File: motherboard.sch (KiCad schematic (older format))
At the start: 90 parts, among them P1 CONN_02X08, U1 STM32F411-LQFP64, U10 74LS125, U11 74LS125, U12 74LS125, U13 74LS125, U14 PCA9517A, U15 PCA9517A, U16 74LS125, U17 74LS125, U2 STM32F411-LQFP64, U3 AP7313, U4 74LS00, U5 74LS125, U6 FM25V20A-G, U7 FM25V20A-G, U8 FM25V20A-G, U9 FM25V20A-G, Y1 32k, Y2 8M(16pF), Y3 32k, Y4 8M(16pF)

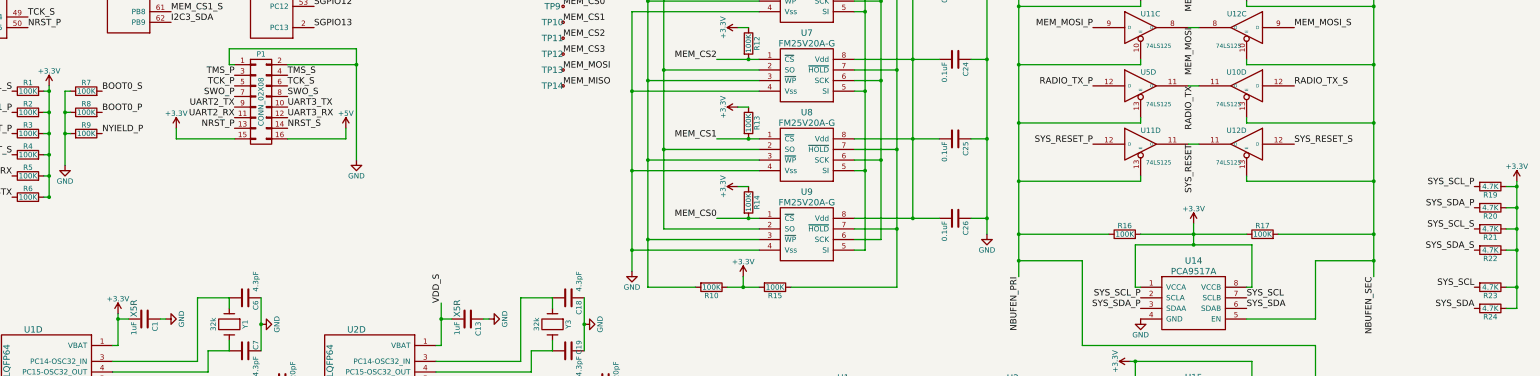
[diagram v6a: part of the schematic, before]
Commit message: Placed all components
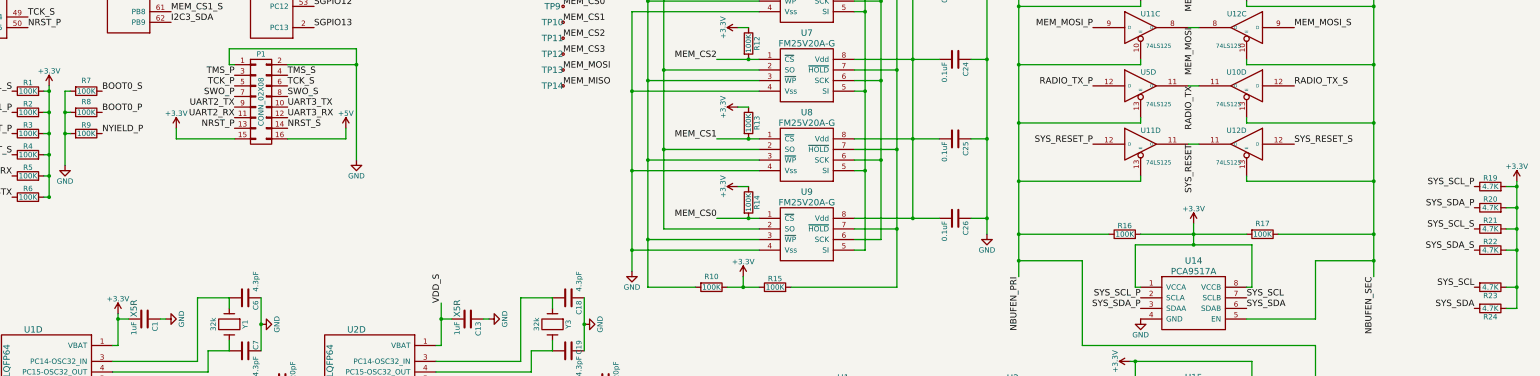
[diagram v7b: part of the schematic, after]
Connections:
- net +3V3: now also R15.1, R17.2, R19.2, R20.2, R21.2, R22.2; no longer R15.2, R17.1, R19.1, R20.1, R21.1, R22.1
- net BOOT0_P: now also R8.1; no longer R8.2
- net BOOT0_S: now also R7.1; no longer R7.2
- net GND: now also R7.2, R8.2; no longer R7.1, R8.1
- net NBUFEN_SEC: now also R17.1; no longer R17.2
- net SYS_SCL_P: now also R19.1; no longer R19.2
- net SYS_SCL_S: now also R21.1; no longer R21.2
- net SYS_SDA_P: now also R20.1; no longer R20.2
- net SYS_SDA_S: now also R22.1; no longer R22.2
- net at U6.7 (~HOLD), U7.7 (~HOLD), U8.7 (~HOLD)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: now also R15.2; no longer R15.1
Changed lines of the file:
@@
 U 1 1 56B9204C
 P 13100 6750
-F 0 "R17" V 13180 6750 50  0000 C CNN
+F 0 "R17" V 13000 6750 50  0000 C CNN
 F 1 "100K" V 13100 6750 50  0000 C CNN
 F 2 "Resistors_SMD:R_0805_HandSoldering" V 13030 6750 30  0001 C CNN
 F 3 "" H 13100 6750 30  0000 C CNN
 	1    13100 6750
-	0    -1   -1   0
+	0    1    1    0
 $EndComp
 $Comp
@@
 U 1 1 56E68F3A
 P 2000 5600
-F 0 "R8" V 2080 5600 50  0000 C CNN
+F 0 "R8" V 1900 5600 50  0000 C CNN
 F 1 "100K" V 2000 5600 50  0000 C CNN
 F 2 "Resistors_SMD:R_0805_HandSoldering" V 1930 5600 30  0001 C CNN
 F 3 "" H 2000 5600 30  0000 C CNN
 	1    2000 5600
-	0    -1   -1   0
+	0    1    1    0
 $EndComp
 $Comp
@@
 U 1 1 56E690F6
 P 2000 5400
-F 0 "R7" V 2080 5400 50  0000 C CNN
+F 0 "R7" V 1900 5400 50  0000 C CNN
 F 1 "100K" V 2000 5400 50  0000 C CNN
 F 2 "Resistors_SMD:R_0805_HandSoldering" V 1930 5400 30  0001 C CNN
 F 3 "" H 2000 5400 30  0000 C CNN
 	1    2000 5400
-	0    -1   -1   0
+	0    1    1    0
 $EndComp
 Text Label 2150 5600 0    60   ~ 0
@@
 F 3 "" H 15250 6300 30  0000 C CNN
 	1    15250 6300
-	0    1    1    0
+	0    -1   -1   0
 $EndComp
 $Comp
@@
 F 3 "" H 15250 6500 30  0000 C CNN
 	1    15250 6500
-	0    1    1    0
+	0    -1   -1   0
 $EndComp
 $Comp
@@
 F 3 "" H 15250 6700 30  0000 C CNN
 	1    15250 6700
-	0    1    1    0
+	0    -1   -1   0
 $EndComp
 $Comp
@@
 F 3 "" H 15250 6900 30  0000 C CNN
 	1    15250 6900
-	0    1    1    0
+	0    -1   -1   0
 $EndComp
 $Comp
@@
 U 1 1 56FFBA91
 P 7900 7250
-F 0 "R10" V 7980 7250 50  0000 C CNN
+F 0 "R10" V 7800 7250 50  0000 C CNN
 F 1 "100K" V 7900 7250 50  0000 C CNN
 F 2 "Resistors_SMD:R_0805_HandSoldering" V 7830 7250 30  0001 C CNN
@@
 F 3 "" H 8500 7250 30  0000 C CNN
 	1    8500 7250
-	0    1    1    0
-$EndComp
-$Comp
+	0    -1   -1   0
+$EndComp
+$Comp

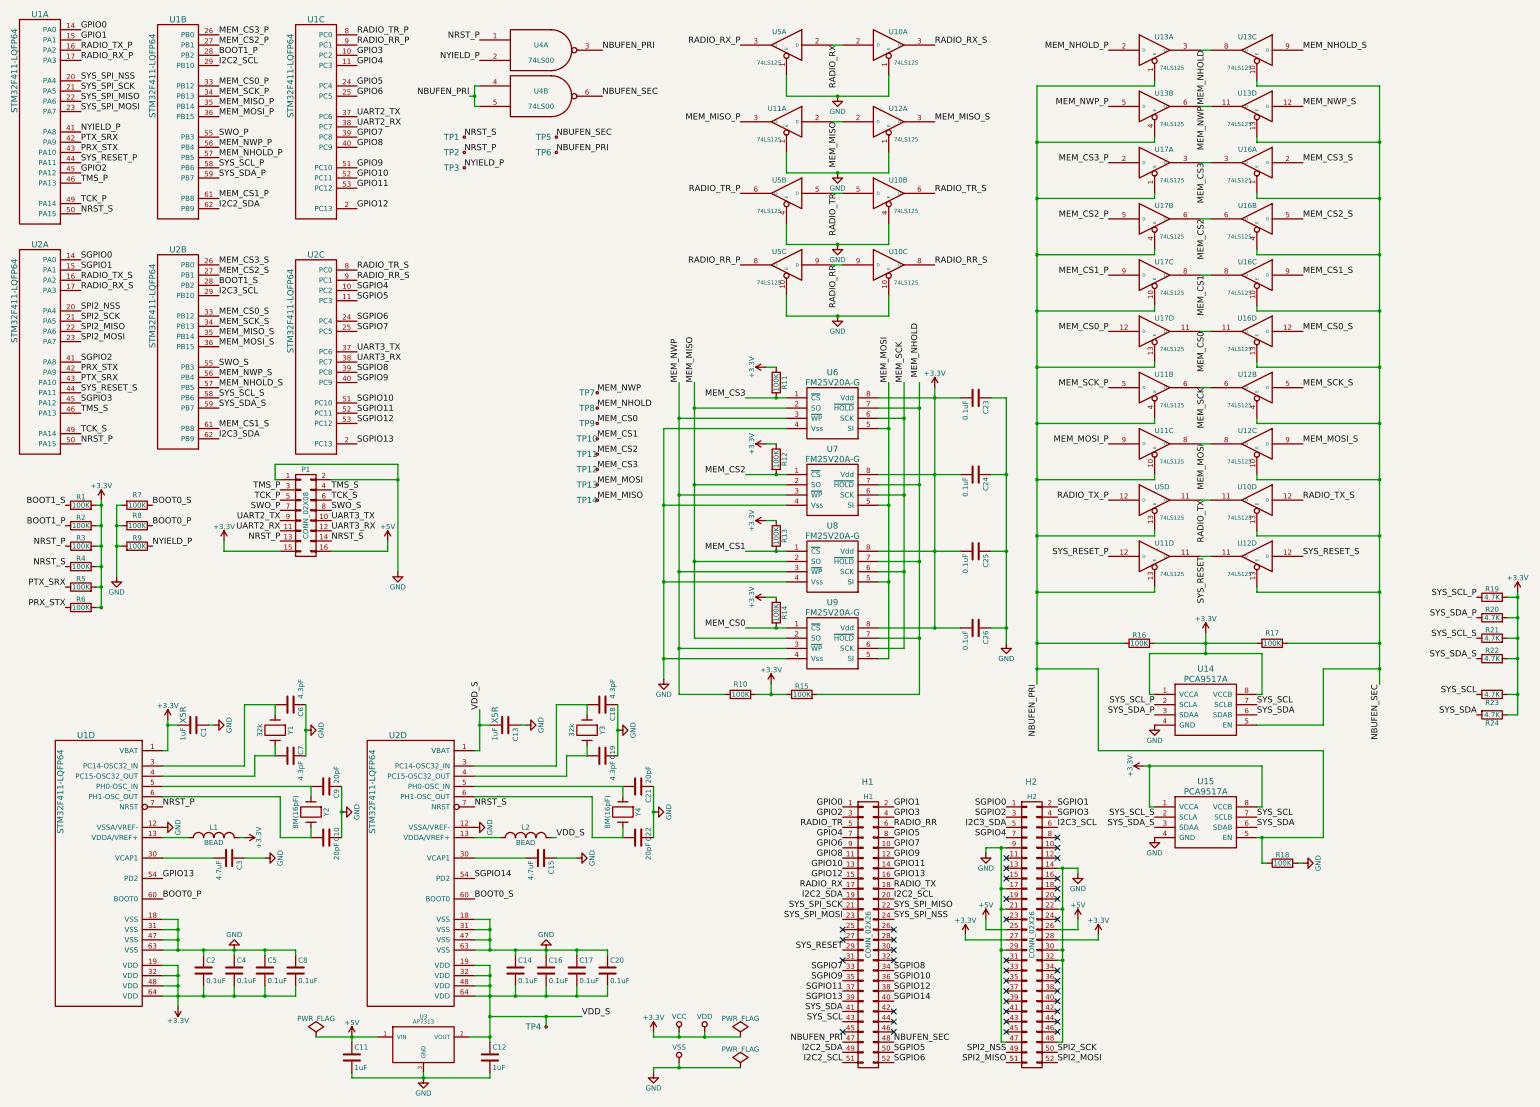
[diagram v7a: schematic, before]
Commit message: Routed P1 High-speed signals
- Main UART
- Main I2C
- Mem SPI
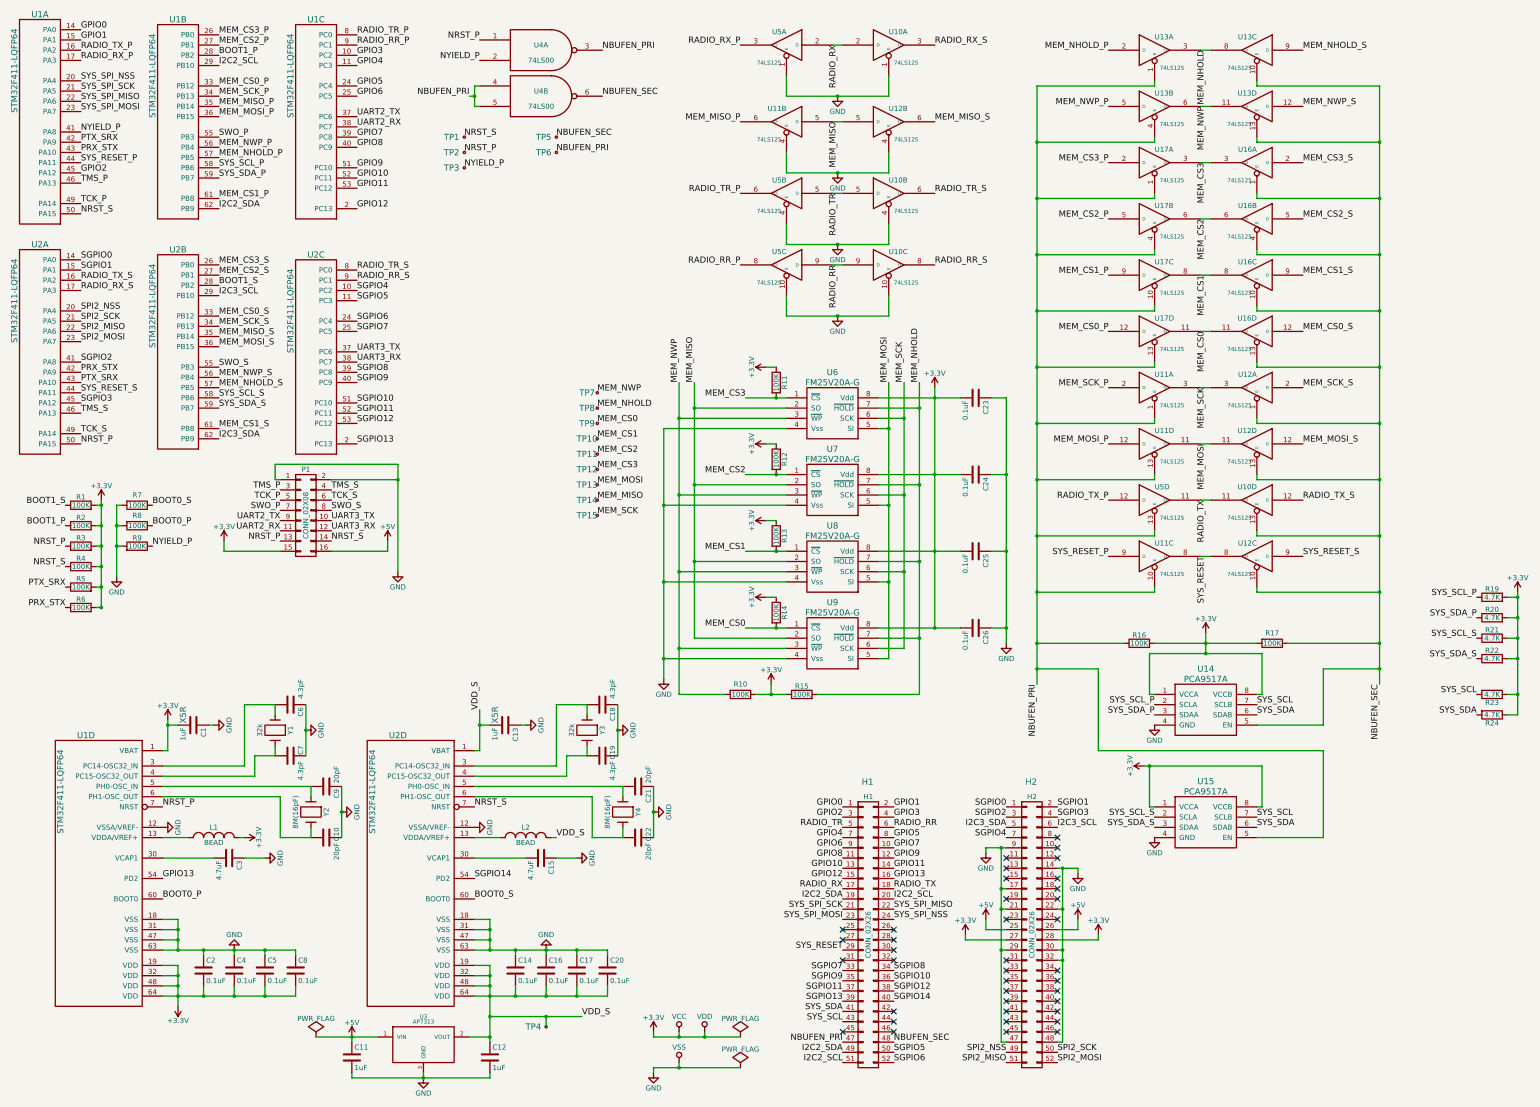
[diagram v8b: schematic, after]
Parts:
- removed R18: 100K, Resistors_SMD:R_0805_HandSoldering, symbol R
- added TP15: TP, motherboard:TP_0603, symbol TP
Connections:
- net GND: now also U11.4 (E), U12.4 (E); no longer U11.1 (E), U12.1 (E)
- net MEM_MISO: now also U11.5 (D), U12.5 (D); no longer U11.2 (D), U12.2 (D)
- net MEM_MISO_P: now also U11.6 (O); no longer U11.3 (O)
- net MEM_MISO_S: now also U12.6 (O); no longer U12.3 (O)
- net MEM_MOSI: now also U11.11 (O), U12.11 (O); no longer U11.8 (O), U12.8 (O)
- net MEM_MOSI_P: now also U11.12 (D); no longer U11.9 (D)
- net MEM_MOSI_S: now also U12.12 (D); no longer U12.9 (D)
- net MEM_NHOLD: now also R15.2, U6.7 (~HOLD), U7.7 (~HOLD), U8.7 (~HOLD), U9.7 (~HOLD)
- net MEM_SCK: now also U11.3 (O), U12.3 (O), TP15.1; no longer U11.6 (O), U12.6 (O)
- net MEM_SCK_P: now also U11.2 (D); no longer U11.5 (D)
- net MEM_SCK_S: now also U12.2 (D); no longer U12.5 (D)
- net NBUFEN_PRI: now also U11.1 (E), U11.10 (E), U11.13 (E); no longer U11.10 (E), U11.13 (E), U11.4 (E)
- net NBUFEN_SEC: now also U12.1 (E), U12.10 (E), U12.13 (E); no longer U12.10 (E), U12.13 (E), U12.4 (E)
- net SYS_RESET: now also U11.8 (O), U12.8 (O); no longer U11.11 (O), U12.11 (O)
- net SYS_RESET_P: now also U11.9 (D); no longer U11.12 (D)
- net SYS_RESET_S: now also U12.9 (D); no longer U12.12 (D)
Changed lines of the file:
@@
 	1    0    0    -1
 $EndComp
-Text Label 9650 4150 1    60   ~ 0
+Text Label 9650 4200 1    60   ~ 0
 MEM_NHOLD
 Text Label 9500 4200 1    60   ~ 0
@@
 	1    0    0    -1
 $EndComp
-$Comp
-L R R18
-U 1 1 56EF0DD7
-P 13200 8900
-F 0 "R18" V 13280 8900 50  0000 C CNN
-F 1 "100K" V 13200 8900 50  0000 C CNN
-F 2 "Resistors_SMD:R_0805_HandSoldering" V 13130 8900 30  0001 C CNN
-F 3 "" H 13200 8900 30  0000 C CNN
-	1    13200 8900
-	0    -1   -1   0
-$EndComp
-$Comp
-L GND #PWR034
-U 1 1 56EF0DDD
-P 13400 8900
-F 0 "#PWR034" H 13400 8650 50  0001 C CNN
-F 1 "GND" H 13400 8750 50  0000 C CNN
-F 2 "" H 13400 8900 60  0000 C CNN
-F 3 "" H 13400 8900 60  0000 C CNN
-	1    13400 8900
-	0    -1   -1   0
-$EndComp
 Text Label 11950 8450 2    60   ~ 0
 SYS_SCL_S
@@
 SYS_SDA_S
 $Comp
-L GND #PWR035
+L GND #PWR034
 U 1 1 56EF0DEA
 P 11950 8650
-F 0 "#PWR035" H 11950 8400 50  0001 C CNN
+F 0 "#PWR034" H 11950 8400 50  0001 C CNN
 F 1 "GND" H 11950 8500 50  0000 C CNN
 F 2 "" H 11950 8650 60  0000 C CNN
@@
 SYS_SDA
 $Comp
-L +3.3V #PWR036
+L +3.3V #PWR035
 U 1 1 56EF1331
 P 11850 7950
-F 0 "#PWR036" H 11850 7800 50  0001 C CNN
+F 0 "#PWR035" H 11850 7800 50  0001 C CNN
 F 1 "+3.3V" H 11850 8090 50  0000 C CNN
 F 2 "" H 11850 7950 60  0000 C CNN
@@
 $EndComp
 $Comp
-L +3.3V #PWR037
+L +3.3V #PWR036
 U 1 1 56F035F5
 P 15500 6250
-F 0 "#PWR037" H 15500 6100 50  0001 C CNN
+F 0 "#PWR036" H 15500 6100 50  0001 C CNN
 F 1 "+3.3V" H 15500 6390 50  0000 C CNN
 F 2 "" H 15500 6250 60  0000 C CNN
@@
 $Comp
 L 74LS125 U11
-U 1 1 56F0C25F
+U 2 1 56F0C25F
 P 8350 1650
 F 0 "U11" H 8350 1750 50  0000 L BNN
@@
 F 2 "Housings_SOIC:SOIC-14_3.9x8.7mm_Pitch1.27mm" H 8350 1650 60  0001 C CNN
 F 3 "" H 8350 1650 60  0000 C CNN
-	1    8350 1650
+	2    8350 1650
 	-1   0    0    -1
 $EndComp
 $Comp
 L 74LS125 U12
-U 1 1 56F0C346
+U 2 1 56F0C346
 P 9350 1650
 F 0 "U12" H 9350 1750 50  0000 L BNN
@@
 F 2 "Housings_SOIC:SOIC-14_3.9x8.7mm_Pitch1.27mm" H 9350 1650 60  0001 C CNN
 F 3 "" H 9350 1650 60  0000 C CNN
-	1    9350 1650
+	2    9350 1650
 	1    0    0    -1
 $EndComp
@@
 $Comp
 L 74LS125 U11
-U 2 1 56F1DA36
+U 1 1 56F1DA36
 P 11950 4250
 F 0 "U11" H 11950 4350 50  0000 L BNN
@@
 F 2 "Housings_SOIC:SOIC-14_3.9x8.7mm_Pitch1.27mm" H 11950 4250 60  0001 C CNN
 F 3 "" H 11950 4250 60  0000 C CNN
-	2    11950 4250
+	1    11950 4250
 	1    0    0    -1
 $EndComp
 $Comp
 L 74LS125 U11
-U 3 1 56F1DB80
+U 4 1 56F1DB80
 P 11950 4800
 F 0 "U11" H 11950 4900 50  0000 L BNN
@@
 F 2 "Housings_SOIC:SOIC-14_3.9x8.7mm_Pitch1.27mm" H 11950 4800 60  0001 C CNN
 F 3 "" H 11950 4800 60  0000 C CNN
-	3    11950 4800
+	4    11950 4800
 	1    0    0    -1
 $EndComp
@@
 $Comp
 L 74LS125 U12
-U 2 1 56F39A21
+U 1 1 56F39A21
 P 12950 4250
 F 0 "U12" H 12950 4350 50  0000 L BNN
@@
 F 2 "Housings_SOIC:SOIC-14_3.9x8.7mm_Pitch1.27mm" H 12950 4250 60  0001 C CNN
 F 3 "" H 12950 4250 60  0000 C CNN
-	2    12950 4250
+	1    12950 4250
 	-1   0    0    -1
 $EndComp
 $Comp
 L 74LS125 U12
-U 3 1 56F39B79
+U 4 1 56F39B79
 P 12950 4800
 F 0 "U12" H 12950 4900 50  0000 L BNN
@@
 F 2 "Housings_SOIC:SOIC-14_3.9x8.7mm_Pitch1.27mm" H 12950 4800 60  0001 C CNN
 F 3 "" H 12950 4800 60  0000 C CNN
-	3    12950 4800
+	4    12950 4800
 	-1   0    0    -1
 $EndComp
@@
 $Comp
 L 74LS125 U11
-U 4 1 56F44FCB
+U 3 1 56F44FCB
 P 11950 5900
 F 0 "U11" H 11950 6000 50  0000 L BNN
@@
 F 2 "Housings_SOIC:SOIC-14_3.9x8.7mm_Pitch1.27mm" H 11950 5900 60  0001 C CNN
 F 3 "" H 11950 5900 60  0000 C CNN
-	4    11950 5900
+	3    11950 5900
 	1    0    0    -1
 $EndComp
 $Comp
 L 74LS125 U12
-U 4 1 56F45134
+U 3 1 56F45134
 P 12950 5900
 F 0 "U12" H 12950 6000 50  0000 L BNN
@@
 F 2 "Housings_SOIC:SOIC-14_3.9x8.7mm_Pitch1.27mm" H 12950 5900 60  0001 C CNN
 F 3 "" H 12950 5900 60  0000 C CNN
-	4    12950 5900
+	3    12950 5900
 	-1   0    0    -1
 $EndComp
@@
 SYS_RESET
 $Comp
-L +3.3V #PWR038
+L +3.3V #PWR037
 U 1 1 56B92E1E
 P 12450 6650
-F 0 "#PWR038" H 12450 6500 50  0001 C CNN
+F 0 "#PWR037" H 12450 6500 50  0001 C CNN
 F 1 "+3.3V" H 12450 6790 50  0000 C CNN
 F 2 "" H 12450 6650 60  0000 C CNN
@@
 NRST_P
 $Comp
-L GND #PWR039
+L GND #PWR038
 U 1 1 56F7245E
 P 4550 6050
-F 0 "#PWR039" H 4550 5800 50  0001 C CNN
+F 0 "#PWR038" H 4550 5800 50  0001 C CNN
 F 1 "GND" H 4550 5900 50  0000 C CNN
 F 2 "" H 4550 6050 60  0000 C CNN
@@
 SGPIO14
 $Comp
-L +5V #PWR040
+L +5V #PWR039
 U 1 1 56FC214F
 P 4100 10600
-F 0 "#PWR040" H 4100 10450 50  0001 C CNN
+F 0 "#PWR039" H 4100 10450 50  0001 C CNN
 F 1 "+5V" H 4100 10740 50  0000 C CNN
 F 2 "" H 4100 10600 60  0000 C CNN
@@
 $EndComp
 $Comp
-L PWR_FLAG #FLG041
+L PWR_FLAG #FLG040
 U 1 1 56FDA5CD
 P 7900 10600
-F 0 "#FLG041" H 7900 10695 50  0001 C CNN
+F 0 "#FLG040" H 7900 10695 50  0001 C CNN
 F 1 "PWR_FLAG" H 7900 10780 50  0000 C CNN
 F 2 "" H 7900 10600 60  0000 C CNN
@@
 $EndComp
 $Comp
-L PWR_FLAG #FLG042
+L PWR_FLAG #FLG041
 U 1 1 56FDB2EA
 P 7900 10900
-F 0 "#FLG042" H 7900 10995 50  0001 C CNN
+F 0 "#FLG041" H 7900 10995 50  0001 C CNN
 F 1 "PWR_FLAG" H 7900 11080 50  0000 C CNN
 F 2 "" H 7900 10900 60  0000 C CNN
@@
 $EndComp
 $Comp
-L PWR_FLAG #FLG043
+L PWR_FLAG #FLG042
 U 1 1 56FE0079
 P 3750 10600
-F 0 "#FLG043" H 3750 10695 50  0001 C CNN
+F 0 "#FLG042" H 3750 10695 50  0001 C CNN
 F 1 "PWR_FLAG" H 3750 10780 50  0000 C CNN
 F 2 "" H 3750 10600 60  0000 C CNN
@@
 $EndComp
 $Comp
-L +3.3V #PWR044
+L +3.3V #PWR043
 U 1 1 56FFD810
 P 8200 7150
-F 0 "#PWR044" H 8200 7000 50  0001 C CNN
+F 0 "#PWR043" H 8200 7000 50  0001 C CNN
 F 1 "+3.3V" H 8200 7290 50  0000 C CNN
 F 2 "" H 8200 7150 60  0000 C CNN
@@
 RADIO_RR_S
 $Comp
-L GND #PWR045
+L GND #PWR044
 U 1 1 583EB3FD
 P 8850 2850
-F 0 "#PWR045" H 8850 2600 50  0001 C CNN
+F 0 "#PWR044" H 8850 2600 50  0001 C CNN
 F 1 "GND" H 8850 2700 50  0000 C CNN
 F 2 "" H 8850 2850 60  0000 C CNN
@@
 $EndComp
 $Comp
-L GND #PWR046
+L GND #PWR045
 U 1 1 583EB403
 P 8850 3550
-F 0 "#PWR046" H 8850 3300 50  0001 C CNN
+F 0 "#PWR045" H 8850 3300 50  0001 C CNN
 F 1 "GND" H 8850 3400 50  0000 C CNN
 F 2 "" H 8850 3550 60  0000 C CNN
@@
 $EndComp
 $Comp
-L +3.3V #PWR047
+L +3.3V #PWR046
 U 1 1 5843537A
 P 2850 5750
-F 0 "#PWR047" H 2850 5600 50  0001 C CNN
+F 0 "#PWR046" H 2850 5600 50  0001 C CNN
 F 1 "+3.3V" H 2850 5890 50  0000 C CNN
 F 2 "" H 2850 5750 50  0000 C CNN
@@
 $EndComp
 $Comp
-L +5V #PWR048
+L +5V #PWR047
 U 1 1 5843721B
 P 4450 5750
-F 0 "#PWR048" H 4450 5600 50  0001 C CNN
+F 0 "#PWR047" H 4450 5600 50  0001 C CNN
 F 1 "+5V" H 4450 5890 50  0000 C CNN
 F 2 "" H 4450 5750 50  0000 C CNN
@@
 	11400 7000 11400 7800
 Wire Wire Line
-	13000 8900 13000 8650
-Wire Wire Line
 	12950 8650 13600 8650
 Wire Wire Line
@@
 	13000 7950 11850 7950
 Connection ~ 11900 7950
-Wire Wire Line
-	13000 8900 13050 8900
-Connection ~ 13000 8650
 Wire Wire Line
 	13600 7000 14150 7000
@@
 	6000 10400 6000 10500
 Connection ~ 6000 10400
-Wire Wire Line
-	13350 8900 13400 8900
 Connection ~ 7550 10600
 Connection ~ 7300 10900
@@
 Connection ~ 10450 8750
 $Comp
-L GND #PWR049
+L GND #PWR048
 U 1 1 5844E13A
 P 10300 8800
-F 0 "#PWR049" H 10300 8550 50  0001 C CNN
+F 0 "#PWR048" H 10300 8550 50  0001 C CNN
 F 1 "GND" H 10300 8650 50  0000 C CNN
 F 2 "" H 10300 8800 60  0000 C CNN
@@
 	11000 8950 11200 8950
 $Comp
-L GND #PWR050
+L GND #PWR049
 U 1 1 5844E529
 P 11200 9000
-F 0 "#PWR050" H 11200 8750 50  0001 C CNN
+F 0 "#PWR049" H 11200 8750 50  0001 C CNN
 F 1 "GND" H 11200 8850 50  0000 C CNN
 F 2 "" H 11200 9000 60  0000 C CNN
@@
 NoConn ~ 11000 9450
 $Comp
-L +5V #PWR051
+L +5V #PWR050
 U 1 1 5844FA31
 P 10300 9450
-F 0 "#PWR051" H 10300 9300 50  0001 C CNN
+F 0 "#PWR050" H 10300 9300 50  0001 C CNN
 F 1 "+5V" H 10300 9590 50  0000 C CNN
 F 2 "" H 10300 9450 60  0000 C CNN
@@
 $EndComp
 $Comp
-L +5V #PWR052
+L +5V #PWR051
 U 1 1 5844FF4E
 P 11200 9450
-F 0 "#PWR052" H 11200 9300 50  0001 C CNN
+F 0 "#PWR051" H 11200 9300 50  0001 C CNN
 F 1 "+5V" H 11200 9590 50  0000 C CNN
 F 2 "" H 11200 9450 60  0000 C CNN
@@
 	10300 9550 10500 9550
 $Comp
-L +3.3V #PWR053
+L +3.3V #PWR052
 U 1 1 5845304F
 P 10100 9600
-F 0 "#PWR053" H 10100 9450 50  0001 C CNN
+F 0 "#PWR052" H 10100 9450 50  0001 C CNN
 F 1 "+3.3V" H 10100 9740 50  0000 C CNN
 F 2 "" H 10100 9600 60  0000 C CNN
@@
 	10100 9650 10100 9600
 $Comp
-L +3.3V #PWR054
+L +3.3V #PWR053
 U 1 1 5845444B
 P 11400 9600
-F 0 "#PWR054" H 11400 9450 50  0001 C CNN
+F 0 "#PWR053" H 11400 9450 50  0001 C CNN
 F 1 "+3.3V" H 11400 9740 50  0000 C CNN
 F 2 "" H 11400 9600 60  0000 C CNN
@@
 Text Label 9400 9950 0    60   ~ 0
 SGPIO8
+$Comp
+L TP TP15
+U 1 1 58940E78
+P 6500 5500
+F 0 "TP15" H 6400 5500 60  0000 C CNN
+F 1 "TP" H 6500 5600 60  0001 C CNN
+F 2 "motherboard:TP_0603" H 6500 5500 60  0001 C CNN
+F 3 "" H 6500 5500 60  0000 C CNN
+	1    6500 5500
+	1    0    0    -1
+$EndComp
+Text Label 6500 5500 0    60   ~ 0
+MEM_SCK
 $EndSCHEMATC
